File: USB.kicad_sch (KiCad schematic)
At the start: 3 parts, among them J1 MUSBRM5C1M0

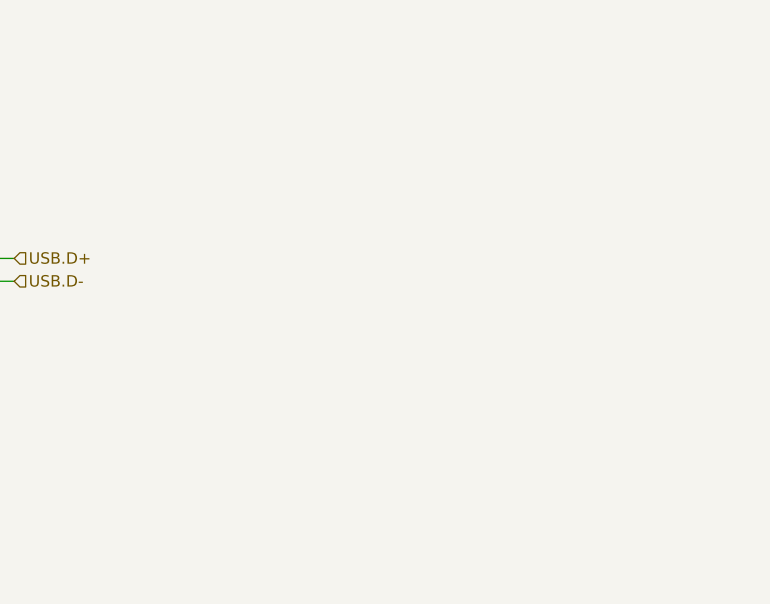
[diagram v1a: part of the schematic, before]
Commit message: Added missing parts of IOcan schematic
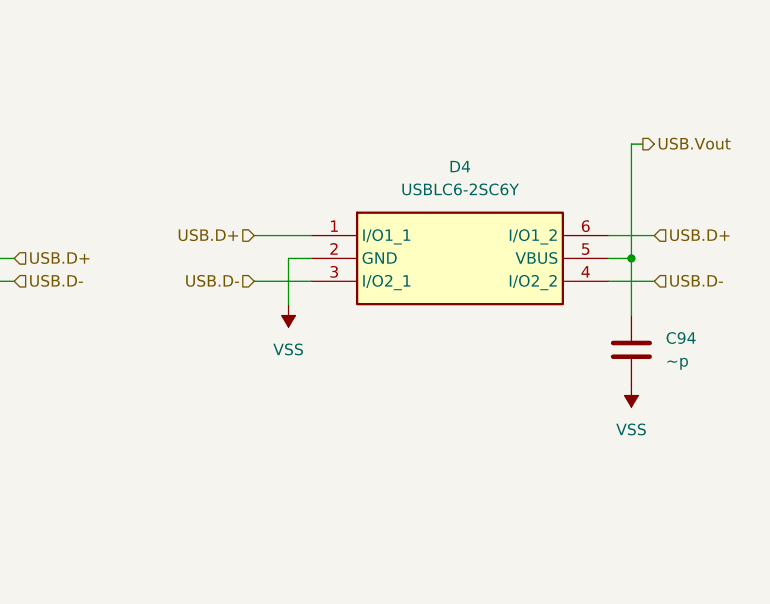
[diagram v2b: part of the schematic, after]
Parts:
- added C94: ~p, Capacitor_SMD:C_0603_1608Metric, symbol Device:C
- added D4: USBLC6-2SC6Y, SOT95P280X145-6N, symbol SamacSys_Parts:USBLC6-2SC6Y
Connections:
- net USB.Vout: now also C94.1, D4.5 (VBUS)
- net VSS: now also C94.2, D4.1 (I/O1_1), D4.2 (GND), D4.3 (I/O2_1), D4.4 (I/O2_2), D4.6 (I/O1_2)

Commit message: Checked pinouts
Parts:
- C94: value ~p -> 100nF/6.3V
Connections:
- net VSS: no longer D4.1 (I/O1_1), D4.3 (I/O2_1), D4.4 (I/O2_2), D4.6 (I/O1_2), J1.A6, J1.A7, J1.B6, J1.B7
- new net USB.D+: D4.1 (I/O1_1), D4.6 (I/O1_2), J1.A6, J1.B6
- new net USB.D-: D4.3 (I/O2_1), D4.4 (I/O2_2), J1.A7, J1.B7
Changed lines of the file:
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@@
-	)
-	(junction
-		(at 137.16 83.82)
-		(diameter 0)
-		(color 0 0 0 0)
 	)
 	(junction
@@
 	)
 	(junction
-		(at 137.16 81.28)
-		(diameter 0)
-		(color 0 0 0 0)
-	)
-	(junction
 		(at 167.64 55.88)
 		(diameter 0)
@@
 	(wire
 		(pts
-			(xy 137.16 81.28) (xy 137.16 83.82)
-		)
-		(stroke
-			(width 0)
-			(type default)
-		)
-	)
-	(wire
-		(pts
 			(xy 168.91 106.68) (xy 168.91 109.22)
 		)
@@
 	(wire
 		(pts
-			(xy 137.16 83.82) (xy 139.7 83.82)
+			(xy 121.92 83.82) (xy 139.7 83.82)
 		)
 		(stroke
@@
 	(wire
 		(pts
-			(xy 137.16 83.82) (xy 137.16 96.52)
-		)
-		(stroke
-			(width 0)
-			(type default)
-		)
-	)
-	(wire
-		(pts
 			(xy 165.1 101.6) (xy 168.91 101.6)
 		)
@@
 	(wire
 		(pts
-			(xy 121.92 83.82) (xy 137.16 83.82)
-		)
-		(stroke
-			(width 0)
-			(type default)
-		)
-	)
-	(wire
-		(pts
 			(xy 134.62 76.2) (xy 139.7 76.2)
 		)
@@
 	(wire
 		(pts
-			(xy 121.92 81.28) (xy 137.16 81.28)
+			(xy 121.92 81.28) (xy 139.7 81.28)
 		)
 		(stroke
@@
 	(wire
 		(pts
-			(xy 137.16 81.28) (xy 139.7 81.28)
-		)
-		(stroke
-			(width 0)
-			(type default)
-		)
-	)
-	(wire
-		(pts
 			(xy 165.1 81.28) (xy 185.42 81.28)
 		)
@@
 	(wire
 		(pts
-			(xy 137.16 68.58) (xy 137.16 81.28)
+			(xy 137.16 68.58) (xy 137.16 96.52)
 		)
 		(stroke
@@
 			)
 		)
-		(property "Value" "~p"
+		(property "Value" "100nF/6.3V"
 			(at 257.81 92.7099 0)
 			(show_name no)
